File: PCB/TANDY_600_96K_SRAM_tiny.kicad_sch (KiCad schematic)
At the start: 5 parts, among them J1 DIN 41612 2x22 male right-ang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, U1 628128_TSOP, U2 74HC148

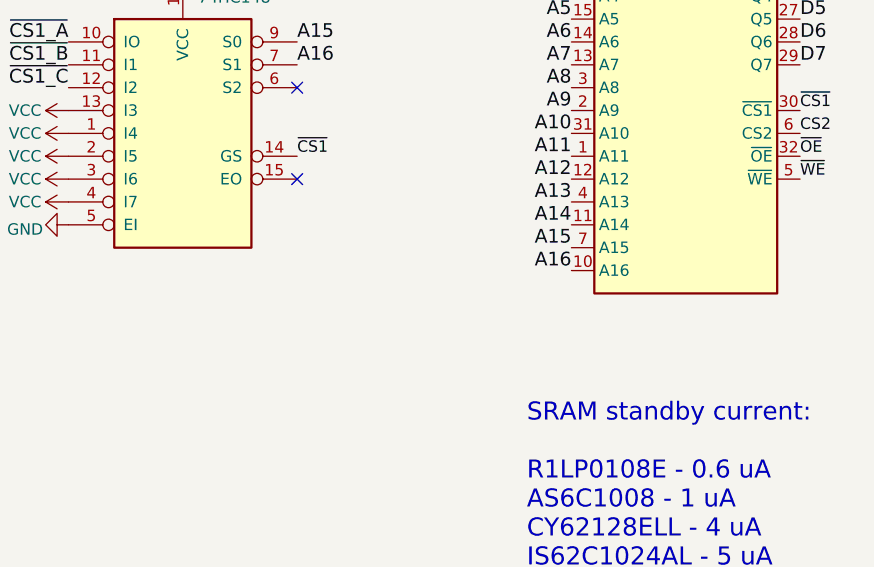
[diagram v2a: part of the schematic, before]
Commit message: re-visible gnd pins on symbols
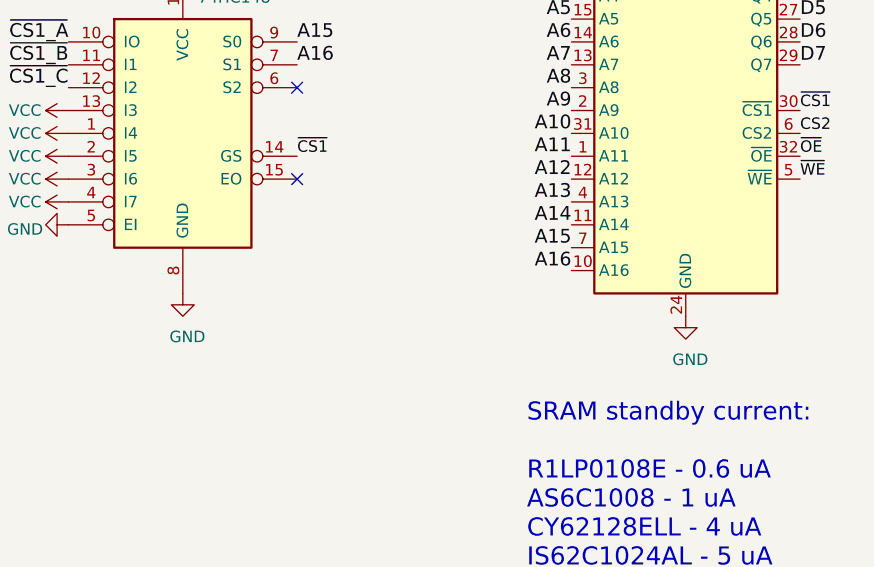
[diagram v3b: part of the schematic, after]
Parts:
- U2: footprint (none) -> 000_LOCAL:SOIC-SOP-16
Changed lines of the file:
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@@
     (property "Reference" "U2" (id 0) (at 129.032 60.96 0))
     (property "Value" "74HC148" (id 1) (at 130.175 63.627 0))
-    (property "Footprint" "" (id 2) (at 124.46 78.74 0)
+    (property "Footprint" "000_LOCAL:SOIC-SOP-16" (id 2) (at 124.46 78.74 0)
       (effects (font (size 1.27 1.27)) hide)
     )
@@
     (pin "1")
   )
+  (symbol (lib_id "000_LOCAL:GND") (at 180.34 99.06 0) (unit 1)
+    (in_bom yes) (on_board yes)
+    (property "Reference" "#PWR?" (id 0) (at 180.34 105.41 0)
+      (effects (font (size 1.27 1.27)) hide)
+    )
+    (property "Value" "GND" (id 1) (at 180.848 103.886 0))
+    (property "Footprint" "" (id 2) (at 180.34 99.06 0)
+      (effects (font (size 1.27 1.27)) hide)
+    )
+    (property "Datasheet" "" (id 3) (at 180.34 99.06 0)
+      (effects (font (size 1.27 1.27)) hide)
+    )
+    (pin "1")
+  )
+  (symbol (lib_id "000_LOCAL:GND") (at 124.46 96.52 0) (unit 1)
+    (in_bom yes) (on_board yes)
+    (property "Reference" "#PWR?" (id 0) (at 124.46 102.87 0)
+      (effects (font (size 1.27 1.27)) hide)
+    )
+    (property "Value" "GND" (id 1) (at 124.968 101.346 0))
+    (property "Footprint" "" (id 2) (at 124.46 96.52 0)
+      (effects (font (size 1.27 1.27)) hide)
+    )
+    (property "Datasheet" "" (id 3) (at 124.46 96.52 0)
+      (effects (font (size 1.27 1.27)) hide)
+    )
+    (pin "1")
+  )
   (sheet_instances
     (path "/" (page "1"))
@@
       (reference "#PWR0127") (unit 1) (value "GND") (footprint "")
     )
+    (path "/74374810-89ba-4a89-82f9-8e20f931d97f"
+      (reference "#PWR?") (unit 1) (value "GND") (footprint "")
+    )
+    (path "/bac393f2-42f7-4a8c-a143-f880697027e5"
+      (reference "#PWR?") (unit 1) (value "GND") (footprint "")
+    )
     (path "/00000000-0000-0000-0000-0000586e7dab"
